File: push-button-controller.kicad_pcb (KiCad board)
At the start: 2 copper layers, 84 parts, among them SW1 SW_Push, SW2 SW_Push, SW3 SW_Push, SW4 SW_Push, U1 LTC2954CTS8-2_TRPBF, U2 LTC2950ITS8-2_TRMPBF, U3 LTC2951ITS8-1, U4 LTC2955CTS8-2_TRPBF

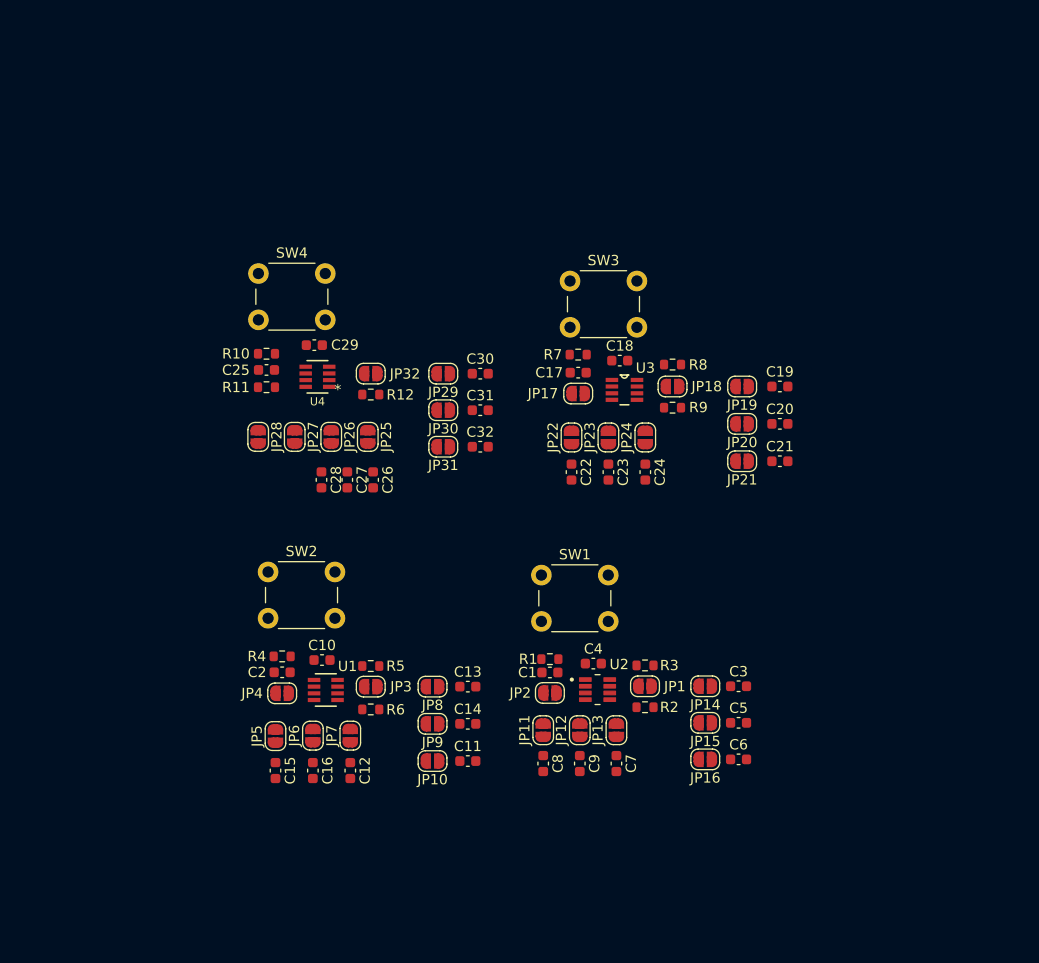
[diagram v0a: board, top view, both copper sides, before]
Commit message: Added B.O.M, TODO: do PCB track layout
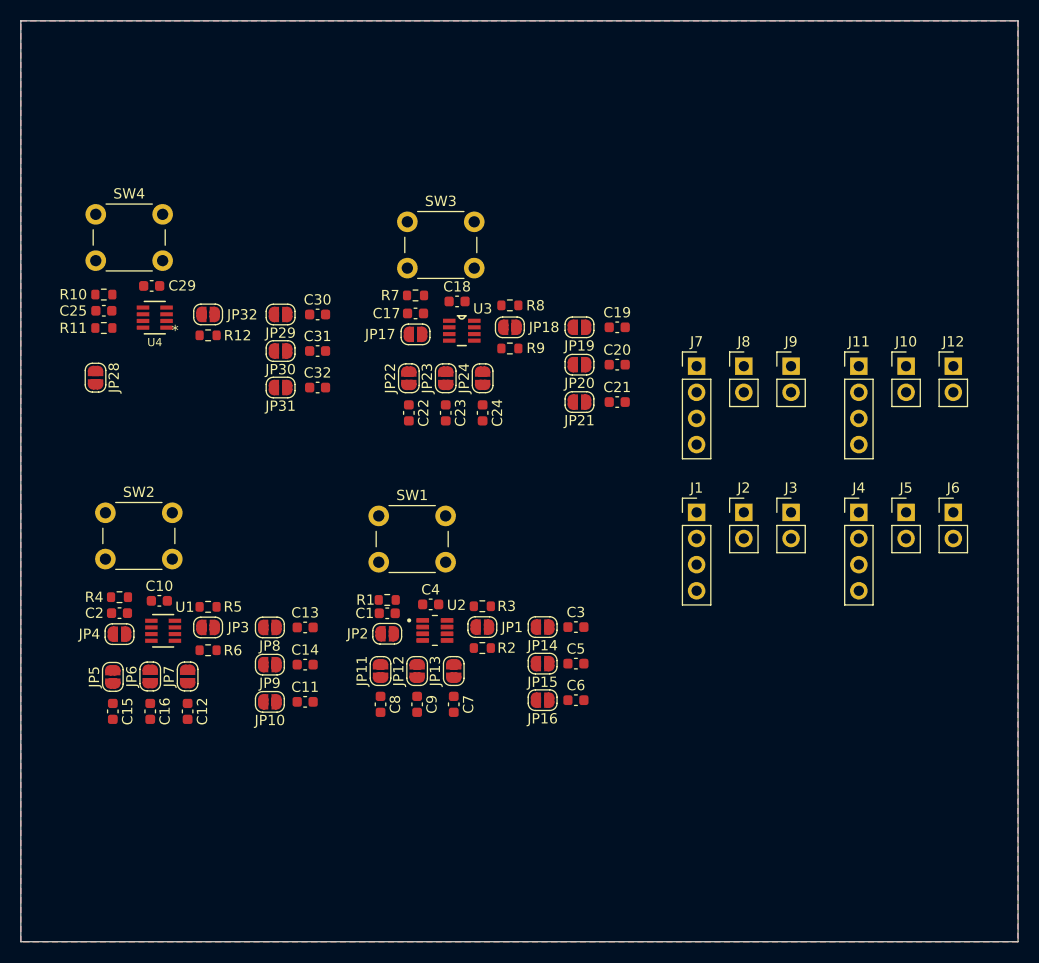
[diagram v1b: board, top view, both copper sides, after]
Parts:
- removed C26, C27, C28: 100nF, Capacitor_SMD:C_0603_1608Metric
- removed JP25, JP26, JP27: JMP2, Jumper:SolderJumper-2_P1.3mm_Open_RoundedPad1.0x1.5mm
- added J1: Conn_01x04, Connector_PinHeader_2.54mm:PinHeader_1x04_P2.54mm_Vertical, F.Cu at (165.4, 97.7)
- added J10: Conn_01x02, Connector_PinHeader_2.54mm:PinHeader_1x02_P2.54mm_Vertical, F.Cu at (185.7, 83.5)
- added J11: Conn_01x04, Connector_PinHeader_2.54mm:PinHeader_1x04_P2.54mm_Vertical, F.Cu at (181.1, 83.5)
- added J12: Conn_01x02, Connector_PinHeader_2.54mm:PinHeader_1x02_P2.54mm_Vertical, F.Cu at (190.3, 83.5)
- added J2: Conn_01x02, Connector_PinHeader_2.54mm:PinHeader_1x02_P2.54mm_Vertical, F.Cu at (169.9, 97.7)
- added J3: Conn_01x02, Connector_PinHeader_2.54mm:PinHeader_1x02_P2.54mm_Vertical, F.Cu at (174.5, 97.7)
- added J4: Conn_01x04, Connector_PinHeader_2.54mm:PinHeader_1x04_P2.54mm_Vertical, F.Cu at (181.1, 97.7)
- added J5: Conn_01x02, Connector_PinHeader_2.54mm:PinHeader_1x02_P2.54mm_Vertical, F.Cu at (185.7, 97.7)
- added J6: Conn_01x02, Connector_PinHeader_2.54mm:PinHeader_1x02_P2.54mm_Vertical, F.Cu at (190.3, 97.7)
- added J7: Conn_01x04, Connector_PinHeader_2.54mm:PinHeader_1x04_P2.54mm_Vertical, F.Cu at (165.4, 83.5)
- added J8: Conn_01x02, Connector_PinHeader_2.54mm:PinHeader_1x02_P2.54mm_Vertical, F.Cu at (169.9, 83.5)
- added J9: Conn_01x02, Connector_PinHeader_2.54mm:PinHeader_1x02_P2.54mm_Vertical, F.Cu at (174.5, 83.5)
- C1, C10, C17, C18, C2, C25, C29, C4: value 100nF -> 100nF/25V
- C11, C21, C31, C6: value 100nF -> 1uF
- C12: value 100nF -> 320
- C13, C19, C24, C3: value 100nF -> 470nF
- C14, C20, C5: value 100nF -> 780nF
- C15, C22, C8: value 100nF -> 78nF
- C16, C23, C9: value 100nF -> 160nF
- C30: value 100nF -> 560nF
- C32: value 100nF -> 1.2uF
- C7: value 100nF -> 320nF
- moved C7 16.8 mm to (141.7, 116.3)
- moved C9 16.8 mm to (138.2, 116.3)
- moved JP17 16.8 mm to (138.0, 80.4)
- moved JP18 16.8 mm to (147.2, 79.7)
- moved JP2 16.8 mm to (135.3, 109.5)
- moved JP22 16.8 mm to (137.4, 84.7)
- moved R7 16.8 mm to (138.0, 76.6)
- moved R8 16.8 mm to (147.2, 77.6)
- moved R9 16.8 mm to (147.2, 81.8)
- moved C1 16.8 mm to (135.3, 107.5)
- moved C17 16.8 mm to (138.0, 78.4)
- moved C22 16.8 mm to (137.4, 88.0)
- moved JP12 16.8 mm to (138.2, 113.1)
- moved JP13 16.8 mm to (141.7, 113.1)
- moved R1 16.8 mm to (135.3, 106.2)
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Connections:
- net Net-(U1-*INT) renamed /LTC2954/*INT
- net Net-(U1-*KILL) renamed /LTC2954/*KILL
- net Net-(U2-~{INT}) renamed /LTC2950/~{INT}
- net Net-(U2-~{KILL}) renamed /LTC2950/~{KILL}
- net Net-(U3-~INT) renamed /LTC2951/~INT
- net Net-(U4-*KILL) renamed /LTC2955/*KILL
- C11 pad 2: unconnected-(C11-Pad2) -> GND
- C12 pad 2: unconnected-(C12-Pad2) -> GND
- C21 pad 2: unconnected-(C21-Pad2) -> GND
- C24 pad 2: unconnected-(C24-Pad2) -> GND
- C32 pad 2: unconnected-(C32-Pad2) -> GND
- C6 pad 2: unconnected-(C6-Pad2) -> GND
- C7 pad 2: unconnected-(C7-Pad2) -> GND
- JP28 pad 1: /LTC2955/CONT -> GND
- JP28 pad 2: unconnected-(JP28-B-Pad2) -> /LTC2955/ON
- U4 pad 1: unconnected-(U4-ON-Pad1) -> /LTC2955/ON
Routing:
- added copper zone on B.Cu, net GND
- added copper zone on F.Cu, net GND
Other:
- board outline added: 96.9 x 89.5 mm

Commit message: Finished, 1st PCB order to JLCPCB
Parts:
- C12: value 320 -> 470nF
- C14, C20, C5: value 780nF -> 820nF
- C15, C22, C8: value 78nF -> 82nF
- C16, C23, C9: value 160nF -> 150nF
- C32: value 1.2uF -> 1.5uF
- C7: value 320nF -> 330nF
- moved J5 81.5 mm to (105.2, 110.5), turned to 180 degrees
- moved J6 70.2 mm to (124.8, 123.2), turned to 180 degrees
- moved J2 68.9 mm to (105.0, 74.8), turned to 180 degrees
- moved J4 59.1 mm to (124.8, 115.6), turned to 180 degrees
- moved J12 51.1 mm to (139.9, 74.8), turned to 180 degrees
- moved J3 49.5 mm to (126.2, 87.3), turned to 180 degrees
- moved J1 43.0 mm to (126.2, 79.9), turned to 180 degrees
- moved J9 42.5 mm to (160.2, 123.5), turned to 180 degrees
- moved JP28 41.8 mm to (146.8, 96.9), turned to 90 degrees
- moved J8 40.2 mm to (140.2, 110.5), turned to 180 degrees
- moved SW4 38.9 mm to (144.4, 79.1), turned to -90 degrees
- moved C29 35.6 mm to (145.4, 88.9)
- moved JP29 35.6 mm to (157.9, 91.7)
- moved JP30 35.6 mm to (157.9, 95.3)
- moved JP31 35.6 mm to (157.9, 98.8)
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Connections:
- C10 pad 1: VIN -> VIN_2954
- C18 pad 1: VIN -> VIN_2951
- C4 pad 1: VIN -> VIN_2950
- J1 pad 1: VPU -> VPU_2951
- J2 pad 1: VIN -> VIN_2951
- J4 pad 1: VPU -> VPU_2954
- J5 pad 1: VIN -> VIN_2954
- J7 pad 1: VPU -> VPU_2950
- J8 pad 1: VIN -> VIN_2950
- R2 pad 2: VPU -> VPU_2950
- R3 pad 2: VPU -> VPU_2950
- R5 pad 2: VPU -> VPU_2954
- R6 pad 2: VPU -> VPU_2954
- R8 pad 2: VPU -> VPU_2951
- R9 pad 2: VPU -> VPU_2951
- U1 pad 1: VIN -> VIN_2954
- U2 pad 1: VIN -> VIN_2950
- U3 pad 1: VIN -> VIN_2951
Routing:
- net /LTC2955/*INT: track 0.00 -> 38.9 mm, vias 0 -> 1
- net VPU: track 0.00 -> 38.2 mm, vias 0 -> 2
- net /LTC2955/EN/~{EN}: track 0.00 -> 37.9 mm, vias 0 -> 1
- net /LTC2955/*KILL: track 0.00 -> 32.2 mm, vias 0 -> 1
- net /LTC2951/~INT: track 0.00 -> 25.3 mm, vias 0 -> 1
- net /LTC2954/*INT: track 0.00 -> 24.9 mm, vias 0 -> 1
- net /LTC2950/~{INT}: track 0.00 -> 24.7 mm, vias 0 -> 1
- net /LTC2951/~KILL: track 0.00 -> 22.9 mm, vias 0 -> 1
- net VPU_2951: track 0.00 -> 22.6 mm, vias 0 -> 2
- net /LTC2950/~{KILL}: track 0.00 -> 22.3 mm, vias 0 -> 1
- net /LTC2954/*KILL: track 0.00 -> 22.3 mm, vias 0 -> 1
- net VPU_2950: track 0.00 -> 22.0 mm, vias 0 -> 2
- net VPU_2954: track 0.00 -> 20.6 mm, vias 0 -> 2
- net VIN: track 0.00 -> 20.3 mm
- net /LTC2951/EN/~{EN}: track 0.00 -> 19.9 mm
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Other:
- board size 96.9 x 89.5 mm -> 66.2 x 72.7 mm
- board text added: "*"
- board text added: "0.5s"
- board text added: "1s"
- board text added: "3s"
- board text added: "5s"
- board text added: "7s"
- board text added: "EN"
- board text added: "GND"
- board text added: "INT"
- board text added: "KILL"
- board text added: "LTC2950"
- board text added: "LTC2951"
- board text added: "LTC2954"
- board text added: "LTC2955"
- board text added: "OFF"
- board text added: "ON"
- board text added: "VIN"
- board text added: "VPU"
